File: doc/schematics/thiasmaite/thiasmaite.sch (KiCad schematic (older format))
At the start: 11 parts

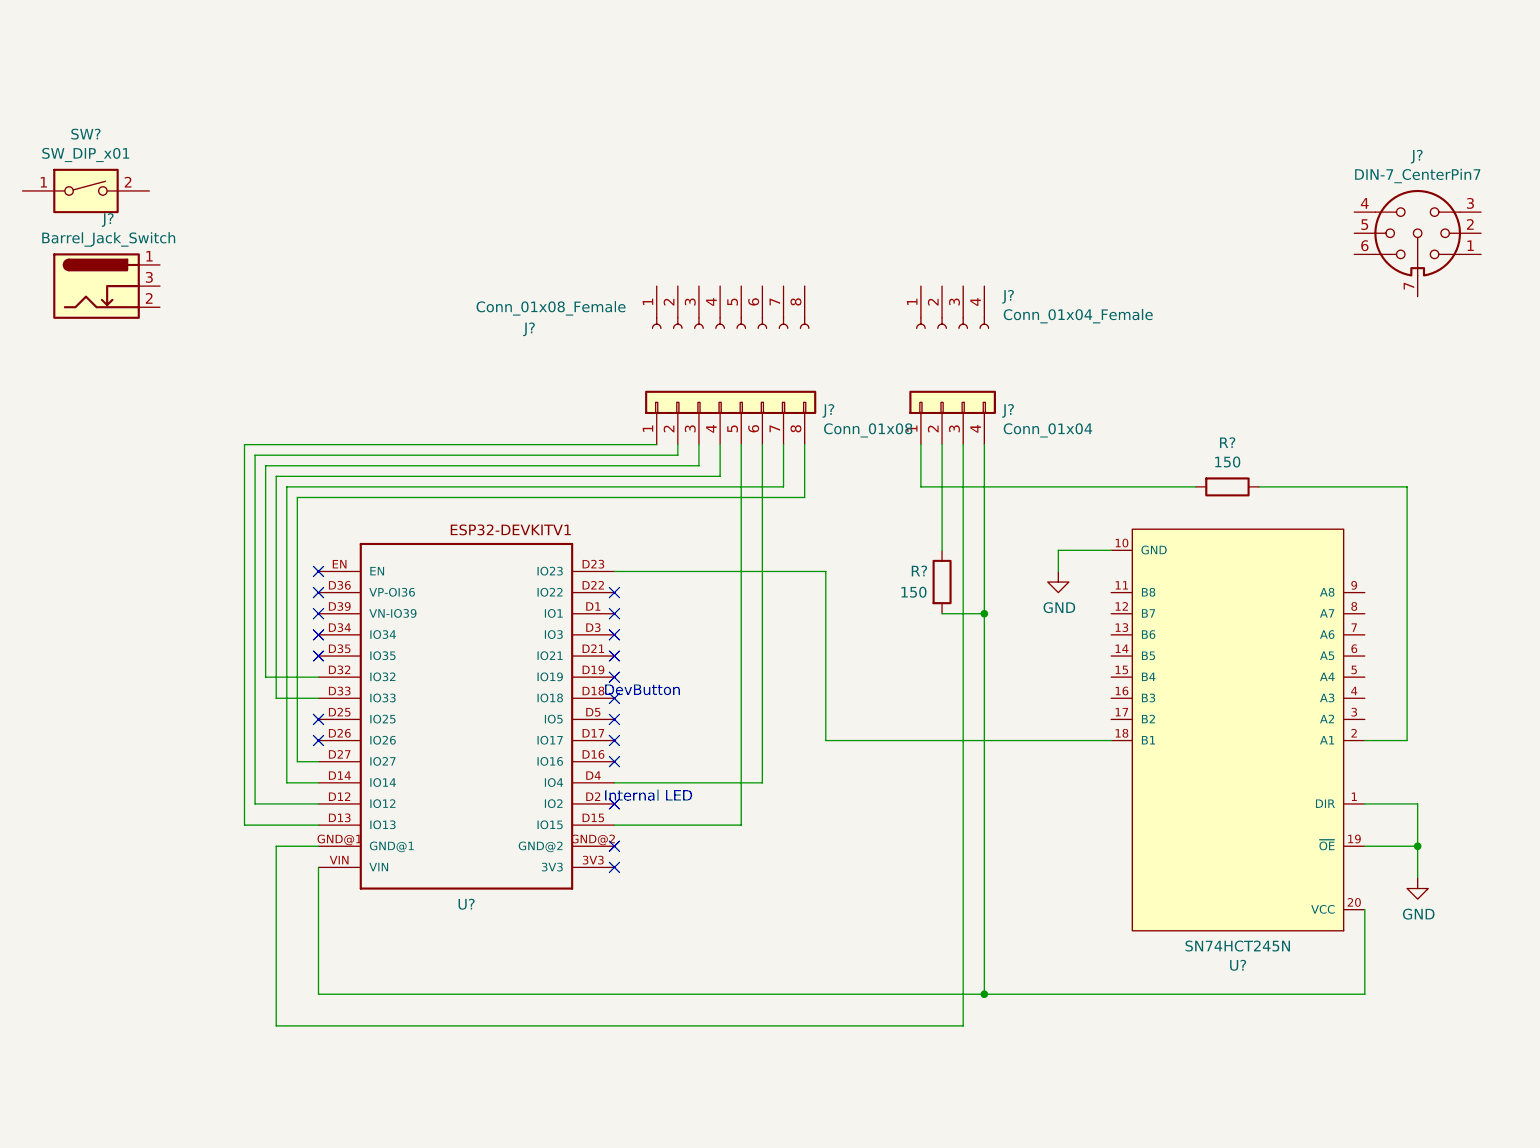
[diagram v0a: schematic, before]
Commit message: Changed connector positions and added pin description
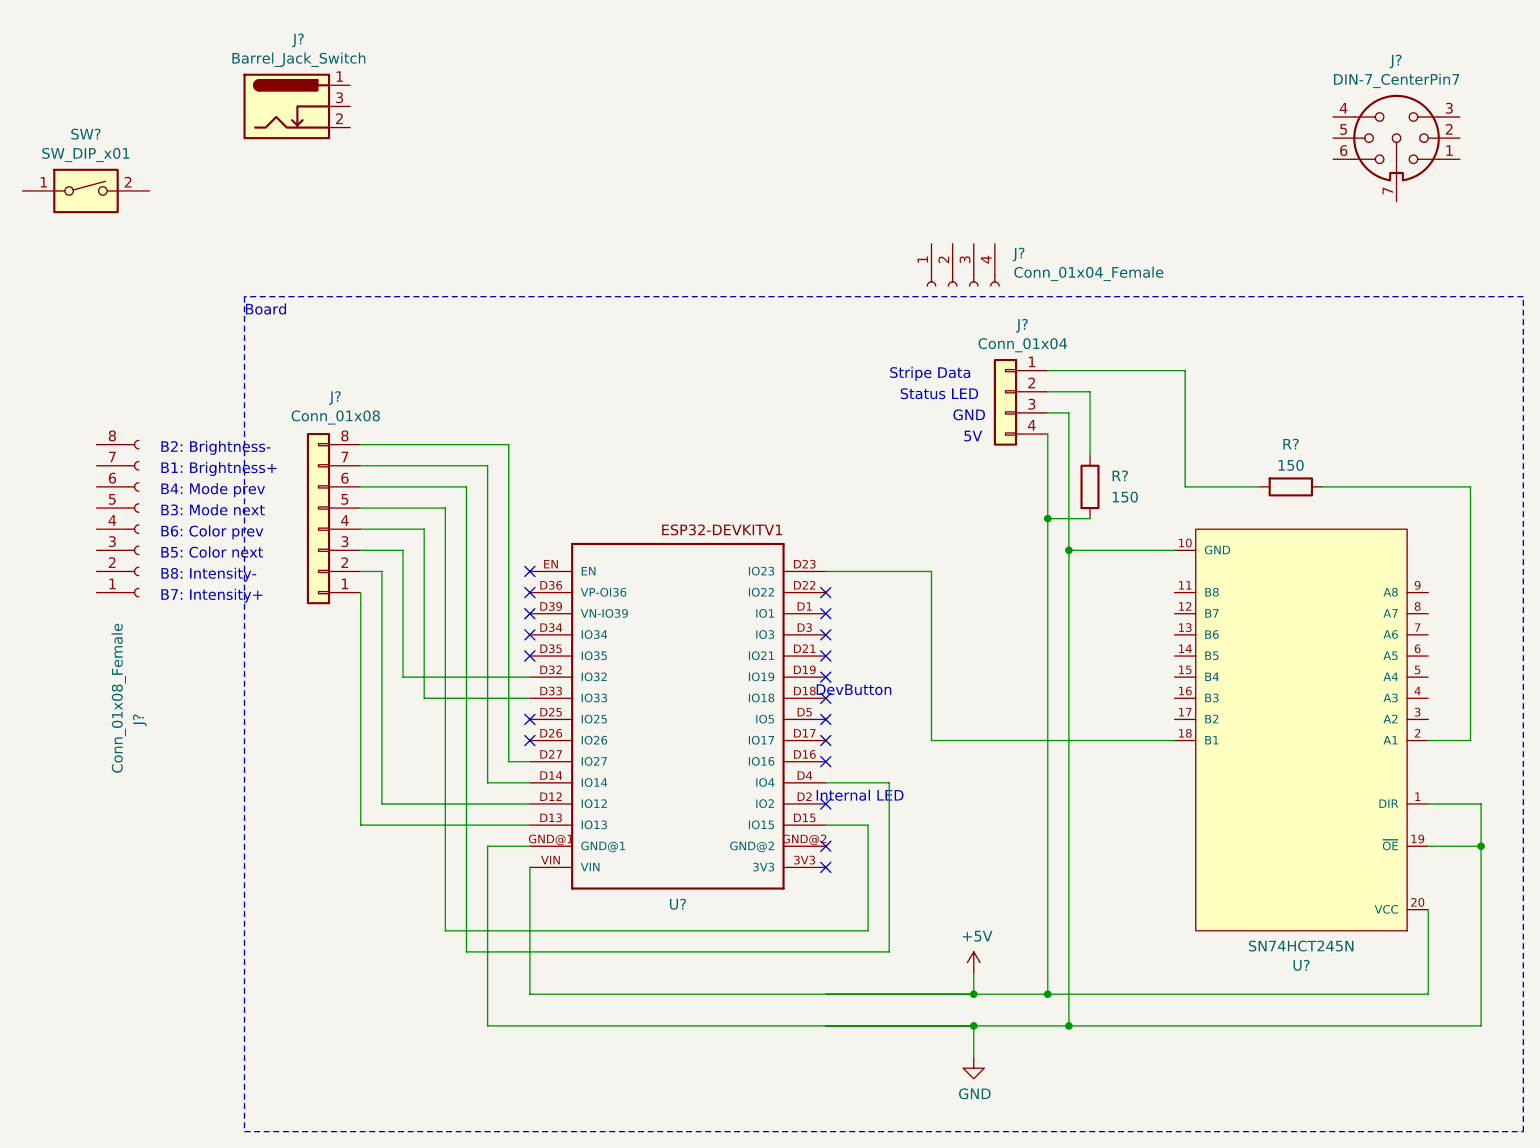
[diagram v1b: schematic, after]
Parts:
- removed J?: Conn_01x08, symbol Connector_Generic:Conn_01x08
- added J?: Conn_01x08, symbol Connector_Generic:Conn_01x08
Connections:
- net labels added: +5V
- wire segments 53 -> 63
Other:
- note added: "5V"
- note added: "B1: Brightness+"
- note added: "B2: Brightness-"
- note added: "B3: Mode next"
- note added: "B4: Mode prev"
- note added: "B5: Color next"
- note added: "B6: Color prev"
- note added: "B7: Intensity+"
- note added: "B8: Intensity-"
- note added: "Board"
- note added: "GND"
- note added: "Status LED"
- note added: "Stripe Data"
- moved on the sheet: J?, R?, U?

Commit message: Added case schematics, finished whole schematics
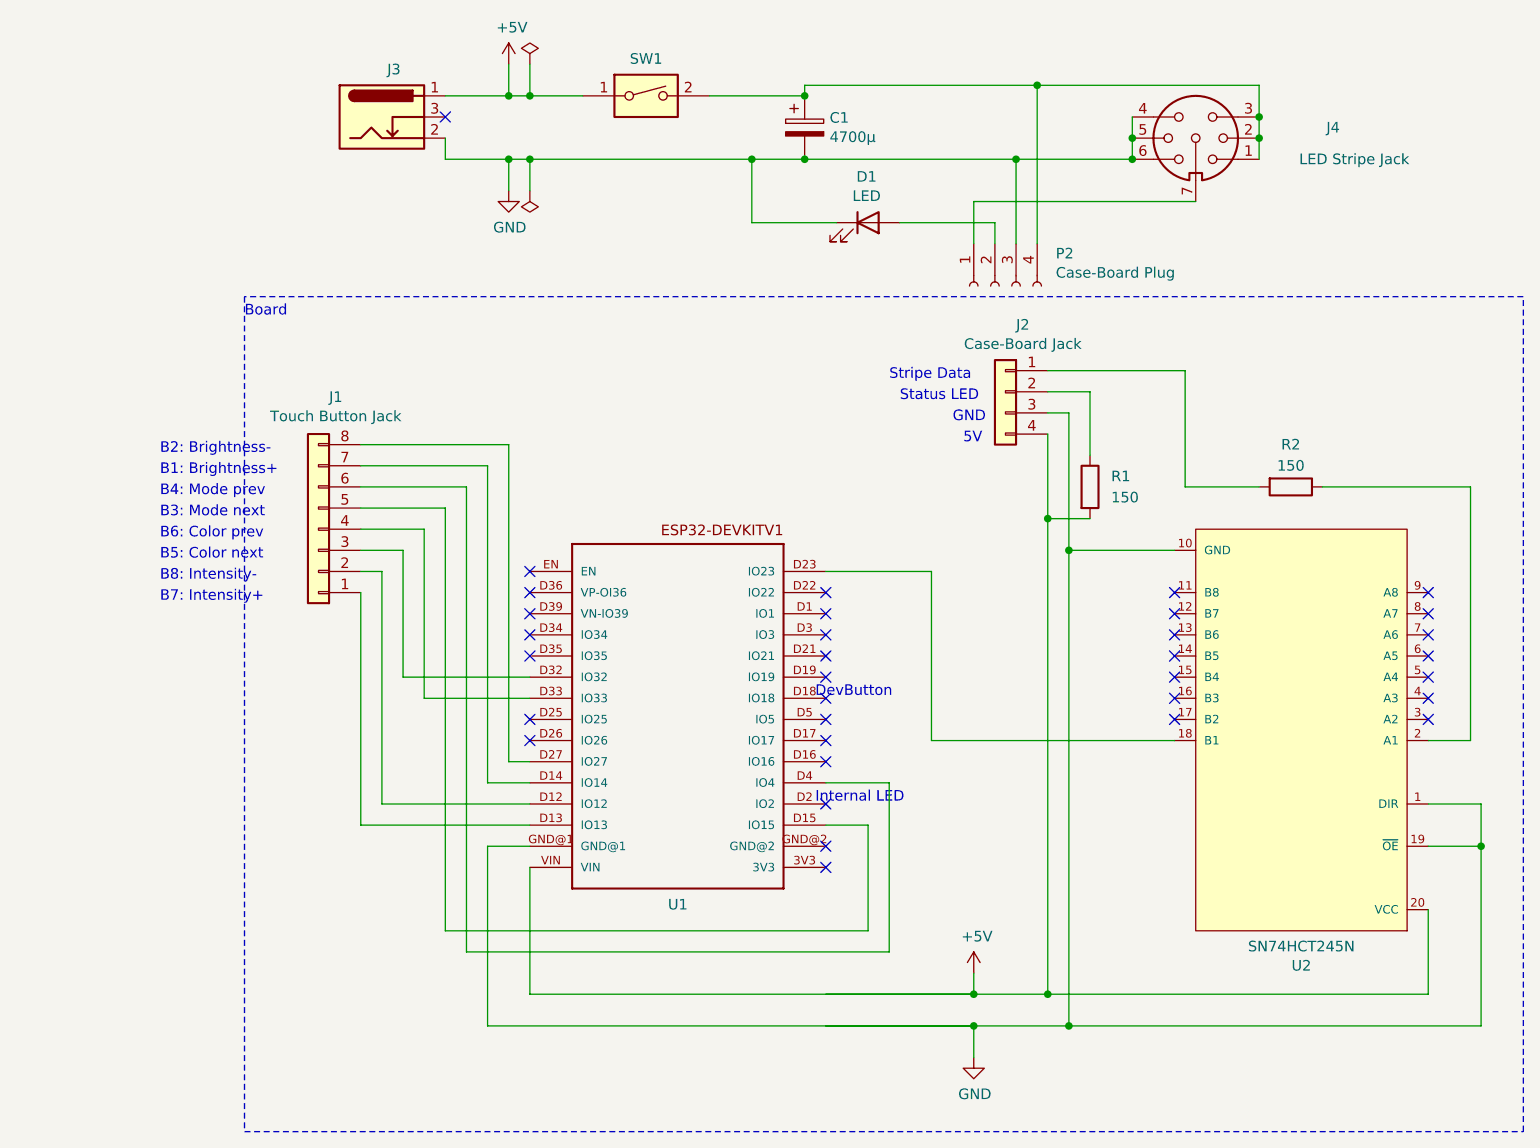
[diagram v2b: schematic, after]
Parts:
- removed J?: Conn_01x08_Female, symbol Connector:Conn_01x08_Female
- added C1: 4700µ, symbol Device:CP
- added D1: LED, symbol Device:LED
- J1: renamed from J?; value Conn_01x08 -> Touch Button Jack
- J2: renamed from J?; value Conn_01x04 -> Case-Board Jack
- J4: renamed from J?; value DIN-7_CenterPin7 -> LED Stripe Jack
- P2: renamed from J?; value Conn_01x04_Female -> Case-Board Plug
- gave numbers to parts that had none: 6
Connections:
- wire segments 63 -> 94
- no-connect marks 19 -> 34
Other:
- moved on the sheet: J3, J4, P2, SW1
